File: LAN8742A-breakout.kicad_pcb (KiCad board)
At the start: 4 copper layers, 40 x 50 mm, 40 parts, among them J1 HR911105A_C12074, J2 J_RMII, J3 J_POW, J4 J_LED, SW1 nRST_SW, U1 LAN8720A, Y1 25MHz

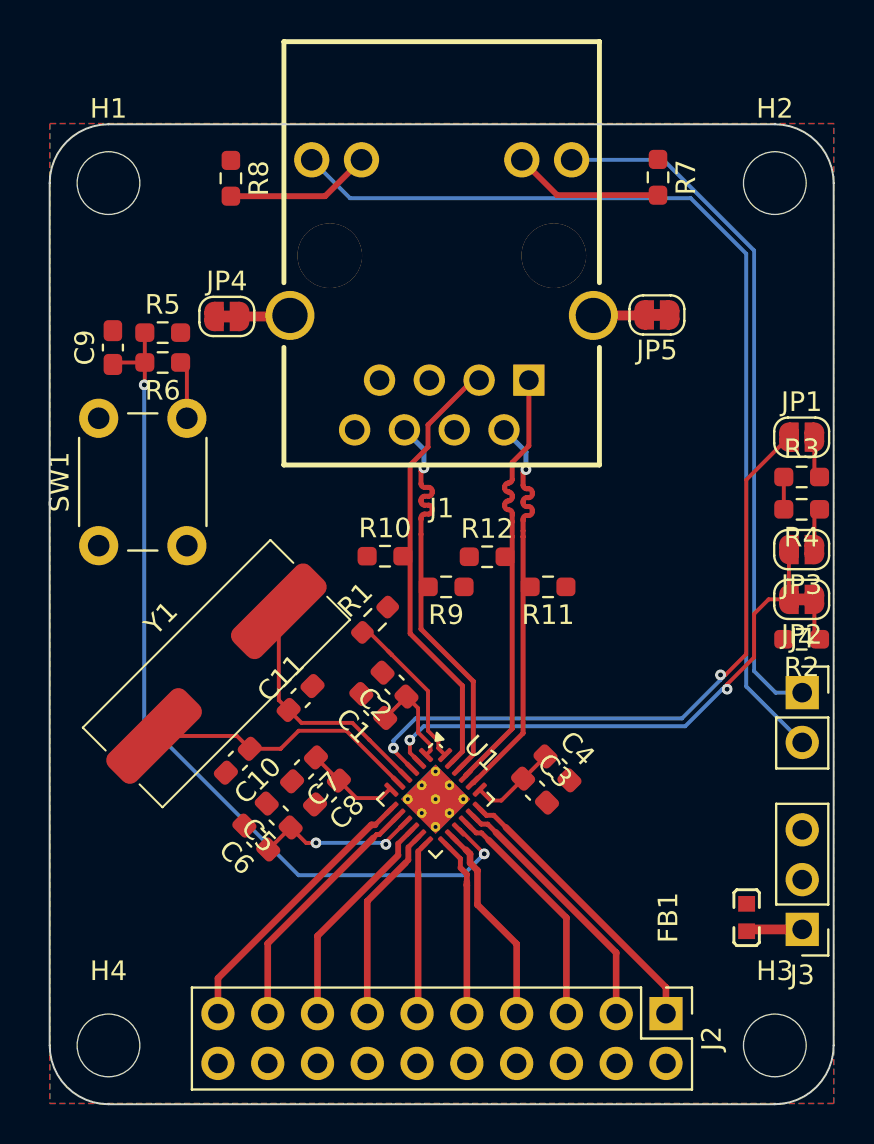
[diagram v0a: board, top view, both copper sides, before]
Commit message: finished routing & added silkscreen
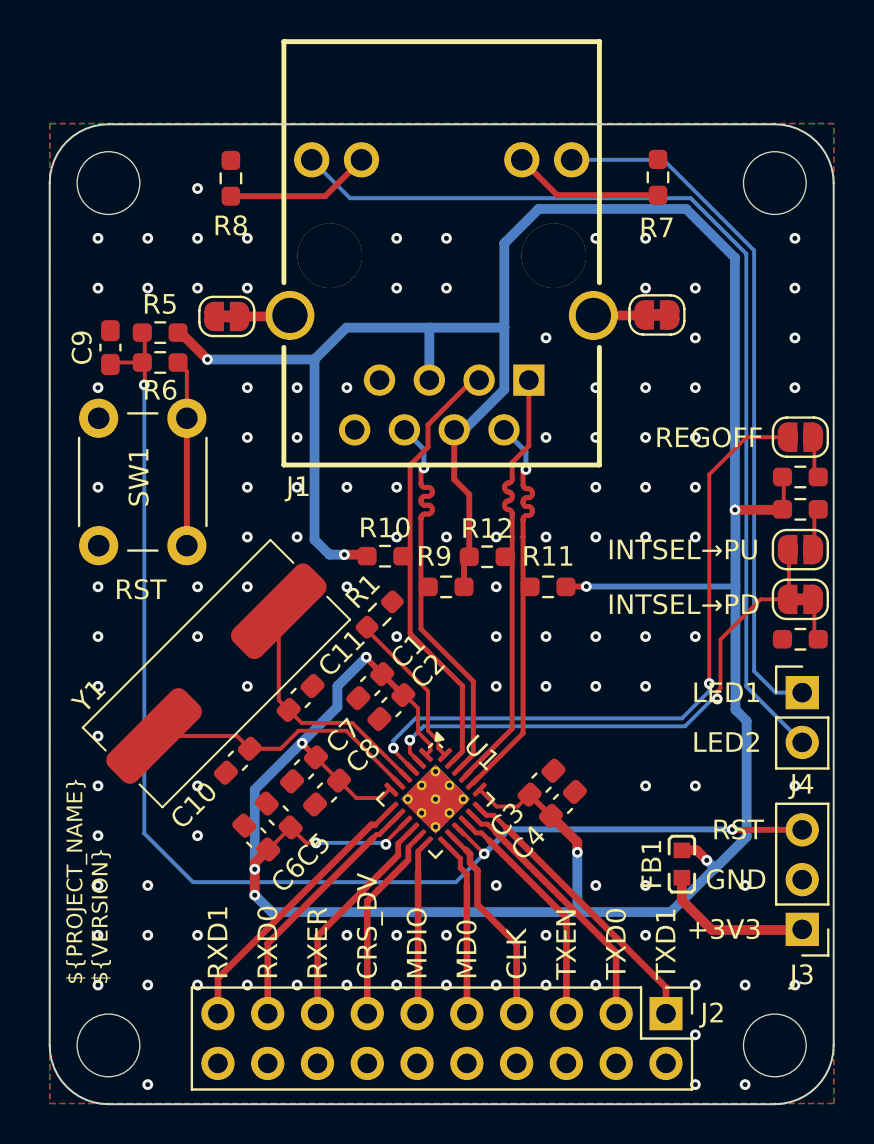
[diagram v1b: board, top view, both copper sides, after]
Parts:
- added G***: LOGO, LOGO, B.Cu at (147.3, 70.1)
- J4: footprint Connector_PinSocket_2.54mm:PinSocket_1x02_P2.54mm_Vertical -> Connector_PinHeader_2.54mm:PinHeader_1x02_P2.54mm_Vertical
- moved FB1 4.28 mm to (159.6, 83.7)
- moved C4 1.83 mm to (153.5, 80.7), turned to 45 degrees
- moved C2 1.16 mm to (144.7, 75.7), turned to -135 degrees
- moved C1 1.03 mm to (143.7, 74.7), turned to -135 degrees
- moved C3 0.52 mm to (152.4, 79.6), turned to 45 degrees
- moved R1 0.35 mm to (144.1, 71.0)
- moved C9 0.13 mm to (130.4, 57.4)
- moved R5 0.13 mm to (132.9, 56.6)
- moved R6 0.13 mm to (132.9, 58.2)
- moved JP1 0.07 mm to (165.6, 62.0)
- moved JP2 0.07 mm to (165.6, 70.2)
- moved JP3 0.07 mm to (165.6, 67.7)
- moved R2 0.07 mm to (165.6, 72.3)
- moved R3 0.07 mm to (165.6, 64.0)
- moved R4 0.07 mm to (165.6, 65.6)
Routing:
- net +3V3_PHYA: track 24.6 -> 183.8 mm, vias 2 -> 12
- net /Project Architecture/LAN8742A breakout/nRST: track 44.4 -> 64.8 mm, vias 2 -> 3
- net Net-(R6-Pad1): track 3.02 -> 9.53 mm
- net +3.3V: track 2.88 -> 7.92 mm
- net Net-(JP1-A): track 33.8 -> 34.9 mm
- net GND: vias 0 -> 112
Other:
- board text added: "${PROJECT_NAME} ${VERSION}"
- board text added: "+3V3"
- board text added: "CLK"
- board text added: "CRS_DV"
- board text added: "GND"
- board text added: "INTSEL→PD"
- board text added: "INTSEL→PU"
- board text added: "LED1"
- board text added: "LED2"
- board text added: "MD0"
- board text added: "MDIO"
- board text added: "REGOFF"
- board text added: "RST"
- board text added: "RXD0"
- board text added: "RXD1"
- board text added: "RXER"
- board text added: "TXD0"
- board text added: "TXD1"
- board text added: "TXEN"
- board text added: "by ${DESIGNER}"

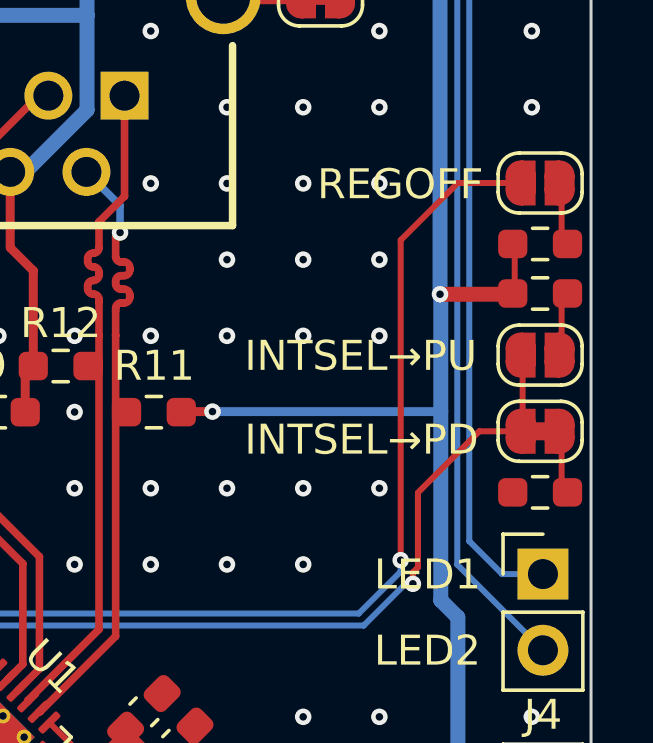
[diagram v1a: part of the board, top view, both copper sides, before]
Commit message: stitching vias
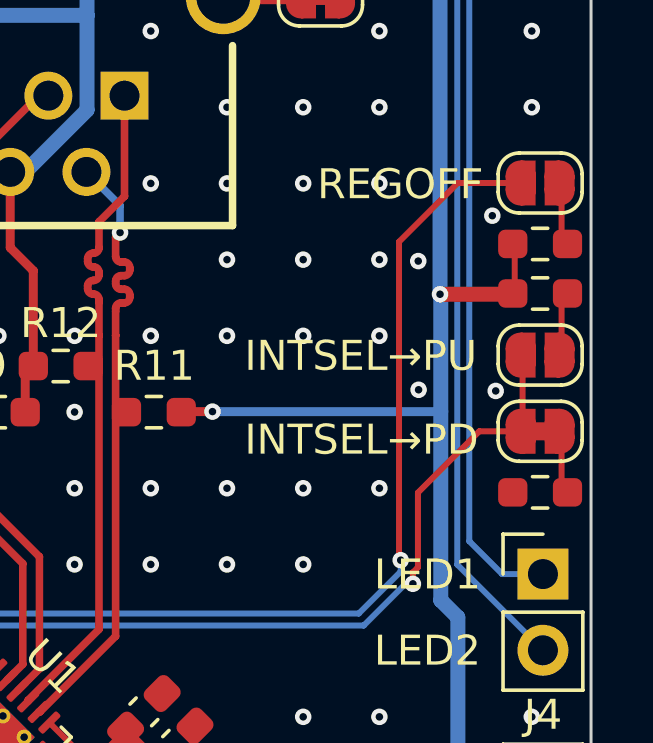
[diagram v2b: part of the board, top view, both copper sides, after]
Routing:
- net GND: vias 112 -> 116
